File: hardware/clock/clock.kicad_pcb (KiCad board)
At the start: 4 copper layers, 106.7 x 76.2 mm, 101 parts, among them J1 Conn_Power, U1 74HC74, U10 74LVC1G38, U11 74LVC1G00, U12 74HC00, U13 74LVC1G38, U14 74HC02, U15 74LVC1G14, U16 74HC4017, U17 74HC4017, U19 74LVC1GX04, U2 74HCS05, U20 74LVC1G04, U21 NE555D, U22 74LVC1G32, U23 74LVC1G04, U24 MIC5504-3.3YM5, U25 74HC08, U26 74LVC2G132, U27 74HC74, U28 74LVC1G02, U29 74HC74, U3 74LVC1G02, U30 74LVC1G04, U4 74HCS05, U5 74LVC1G38, U6 74LVC2G74, U7 74LVC1G08, U8 74HC74, U9 74HCS05, Y1 Crystal

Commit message: Updated schematics and pcbs
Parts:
- removed C24: 100n, Capacitor_SMD:C_0805_2012Metric_Pad1.18x1.45mm_HandSolder
- added C18: 100n, Capacitor_SMD:C_0805_2012Metric_Pad1.18x1.45mm_HandSolder, B.Cu at (108.6, 146.1)
- added D2: LED, LED_SMD:LED_0805_2012Metric_Pad1.15x1.40mm_HandSolder, F.Cu at (98.4, 143.5)
- added D3: LED, LED_SMD:LED_0805_2012Metric_Pad1.15x1.40mm_HandSolder, F.Cu at (98.4, 146.1)
- added J2: Conn_01x03, Connector_PinHeader_2.54mm:PinHeader_1x03_P2.54mm_Vertical, F.Cu at (84.5, 101.6)
- added J3: Conn_01x02_Male, Connector_PinHeader_2.54mm:PinHeader_1x02_P2.54mm_Horizontal, F.Cu at (140.4, 115.6)
- added J4: Conn_01x02_Male, Connector_PinHeader_2.54mm:PinHeader_1x02_P2.54mm_Horizontal, F.Cu at (140.4, 136.5)
- added J5: Conn_01x10_Male, Connector_IDC:IDC-Header_2x05_P2.54mm_Vertical, F.Cu at (84.5, 145.4)
- added R27: 330, Resistor_SMD:R_0805_2012Metric_Pad1.20x1.40mm_HandSolder, B.Cu at (98.4, 143.5)
- added R28: 330, Resistor_SMD:R_0805_2012Metric_Pad1.20x1.40mm_HandSolder, B.Cu at (98.4, 146.1)
- added SW1: SW_Push_4pin, riscv-serial:SW_SPST_DTSM-6, F.Cu at (92.1, 82.5)
- added SW2: SW_Push_4pin, riscv-serial:SW_SPST_DTSM-6, F.Cu at (102.2, 82.5)
- added SW3: SW_Push_4pin, riscv-serial:SW_SPST_DTSM-6, F.Cu at (112.4, 82.5)
- added SW4: SW_Push_4pin, riscv-serial:SW_SPST_DTSM-6, F.Cu at (122.6, 82.5)
- added SW5: SW_Push_4pin, riscv-serial:SW_SPST_DTSM-6, F.Cu at (132.1, 82.5)
- added SW6: SW_Push_4pin, riscv-serial:SW_SPST_DTSM-6, F.Cu at (72.4, 132.1)
- added SW7: SW_Push_4pin, riscv-serial:SW_SPST_DTSM-6, F.Cu at (62.2, 85.7)
- added SW8: SW_Push_4pin, riscv-serial:SW_SPST_DTSM-6, F.Cu at (52.1, 85.7)
- added U18: 74LVC2G04, Package_TO_SOT_SMD:SOT-23-6_Handsoldering, B.Cu at (105.4, 144.8)
- C1, C10, C11, C12, C13, C14, C15, C16, C17, C19, C20, C21, C22, C23, C26, C27, C28, C29, C3, C30, C40, C41, C5, C6, C7, C8, J1, U24: moved to B.Cu
- moved J1 180.8 mm to (51.4, 139.1), turned to 90 degrees
- moved U24 166.2 mm to (64.1, 139.1)
- moved C40 166.0 mm to (59.7, 139.1), turned to 90 degrees
- moved C41 154.8 mm to (67.9, 139.1), turned to 90 degrees
- moved RV1 14.6 mm to (78.1, 91.8)
- moved R17 12.5 mm to (132.1, 91.4)
- moved C35 12.5 mm to (133.3, 94.8)
- moved R16 12.5 mm to (130.8, 94.9)
- moved C34 11.5 mm to (123.8, 94.8)
- moved R14 11.5 mm to (121.3, 94.9)
- moved R15 11.5 mm to (122.6, 91.4)
- moved C33 9.61 mm to (113.7, 94.8)
- moved R12 9.61 mm to (111.1, 94.9)
- moved R13 9.61 mm to (112.4, 91.4)
- moved R9 8.72 mm to (102.2, 90.8)
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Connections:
- U10 pad 1: /STEPDONE -> /STEP_DONE
- U5 pad 1: /OPDONE -> /OP_DONE
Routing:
- net /~{SLEEP}: track 15.4 -> 91.9 mm
- net /STEP_DONE: track 0.00 -> 44.5 mm, vias 0 -> 1
- net /~{CLK}: track 10.6 -> 48.5 mm, vias 0 -> 1
- net GND: track 98.7 -> 136.5 mm, vias 54 -> 51
- net /OP_DONE: track 0.00 -> 37.4 mm, vias 0 -> 1
- net /CLK: track 8.83 -> 46.1 mm, vias 0 -> 1
- net /~{RESET}: track 19.6 -> 46.1 mm
- net /B_OSC: track 10.6 -> 27.7 mm
- net /~{WAIT}: track 35.5 -> 18.6 mm
- net /B_555: track 9.89 -> 26.6 mm
- net /V_IN: track 0.00 -> 16.0 mm
- net /B_STOP: track 37.9 -> 51.3 mm, vias 0 -> 2
- net /B_RESET: track 0.00 -> 11.4 mm
- net Net-(C37-Pad1): track 15.2 -> 26.3 mm
- net Net-(R6-Pad2): track 0.00 -> 9.75 mm
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- added copper zone on B.Cu, net /V_IN
- added copper zone on B.Cu, net VCC
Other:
- board size 106.7 x 76.2 mm -> 99.1 x 76.2 mm
- board text added: "CLK"
- board text added: "~{CLK}"

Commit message: Updated PCBs
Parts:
- moved J5 19.6 mm to (100.3, 156.8)
- moved D2 1.91 mm to (96.5, 143.5)
- moved D3 1.91 mm to (96.5, 146.1)
- moved R27 1.91 mm to (96.5, 143.5)
- moved R28 1.91 mm to (96.5, 146.1)
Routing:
- net GND: track 136.5 -> 173.1 mm, vias 51 -> 60
- net /~{RESET}: track 46.1 -> 71.2 mm
- net /~{CLK}: track 48.5 -> 32.6 mm
- net /CLK: track 46.1 -> 30.7 mm
- net /~{SLEEP}: track 91.9 -> 79.7 mm
- net VCC: track 205.8 -> 217.8 mm, vias 44 -> 49
- net /OP_DONE: track 37.4 -> 45.7 mm
- net /STEP_DONE: track 44.5 -> 51.6 mm
- net Net-(D3-Pad1): track 3.05 -> 0.00 mm
- net Net-(D2-Pad1): track 3.05 -> 0.00 mm
- net Net-(R28-Pad2): track 5.07 -> 6.97 mm
- net Net-(R27-Pad2): track 8.49 -> 10.4 mm
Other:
- board size 99.1 x 76.2 mm -> 99.1 x 99.1 mm

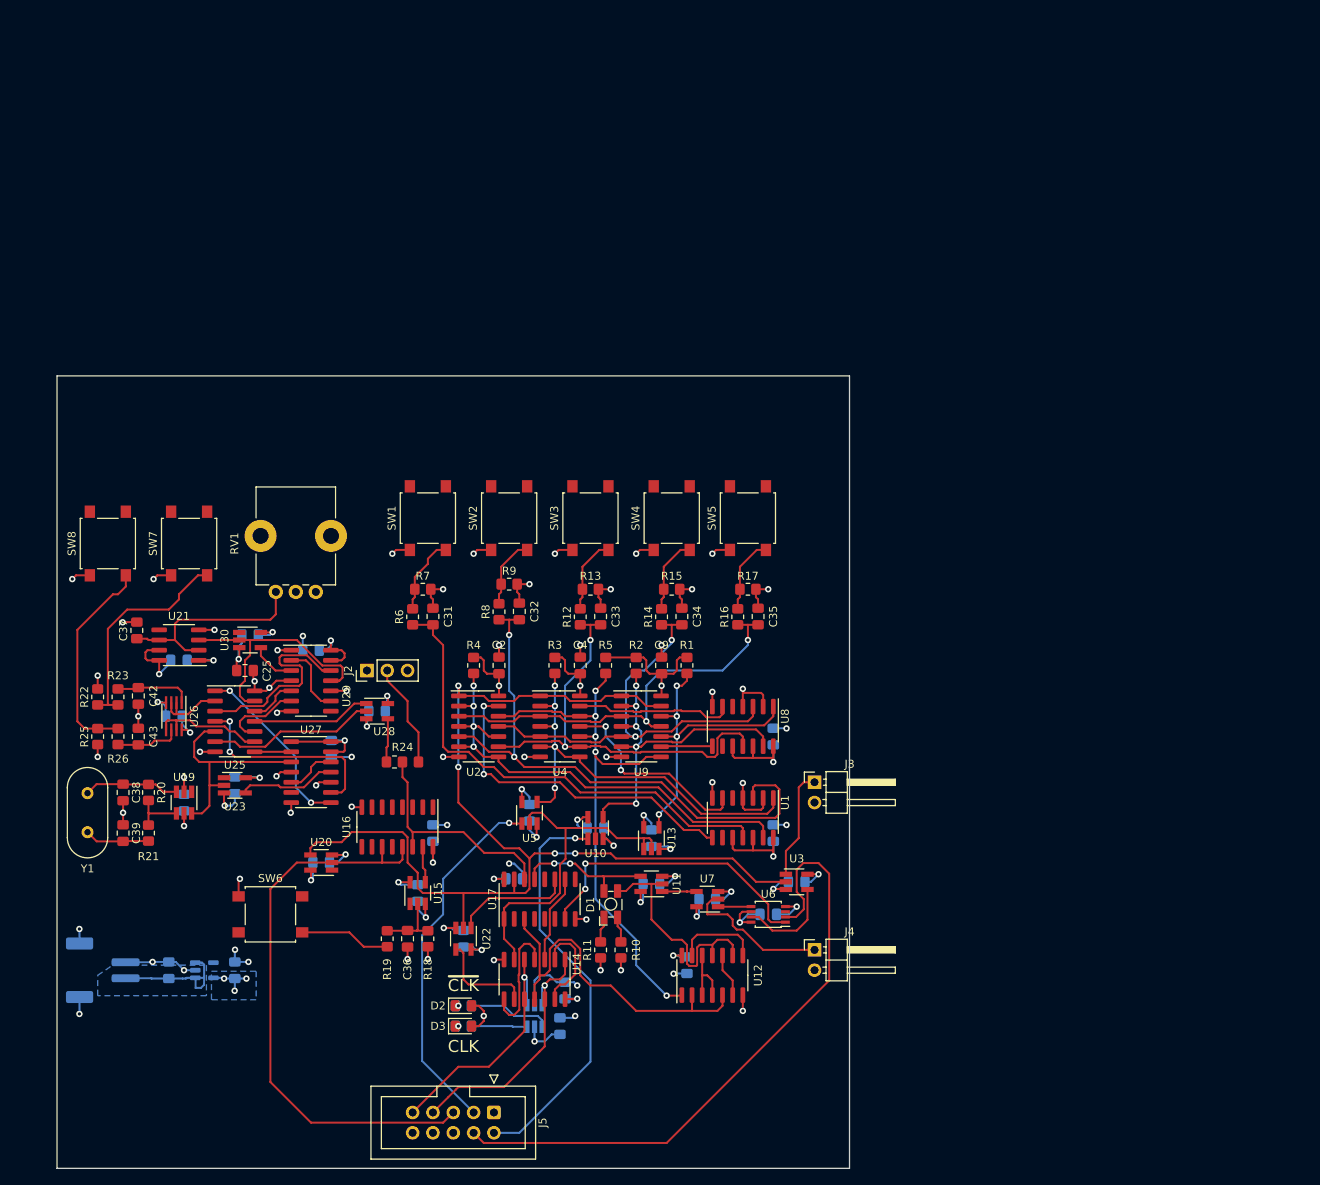
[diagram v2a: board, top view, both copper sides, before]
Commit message: Added two LEDs
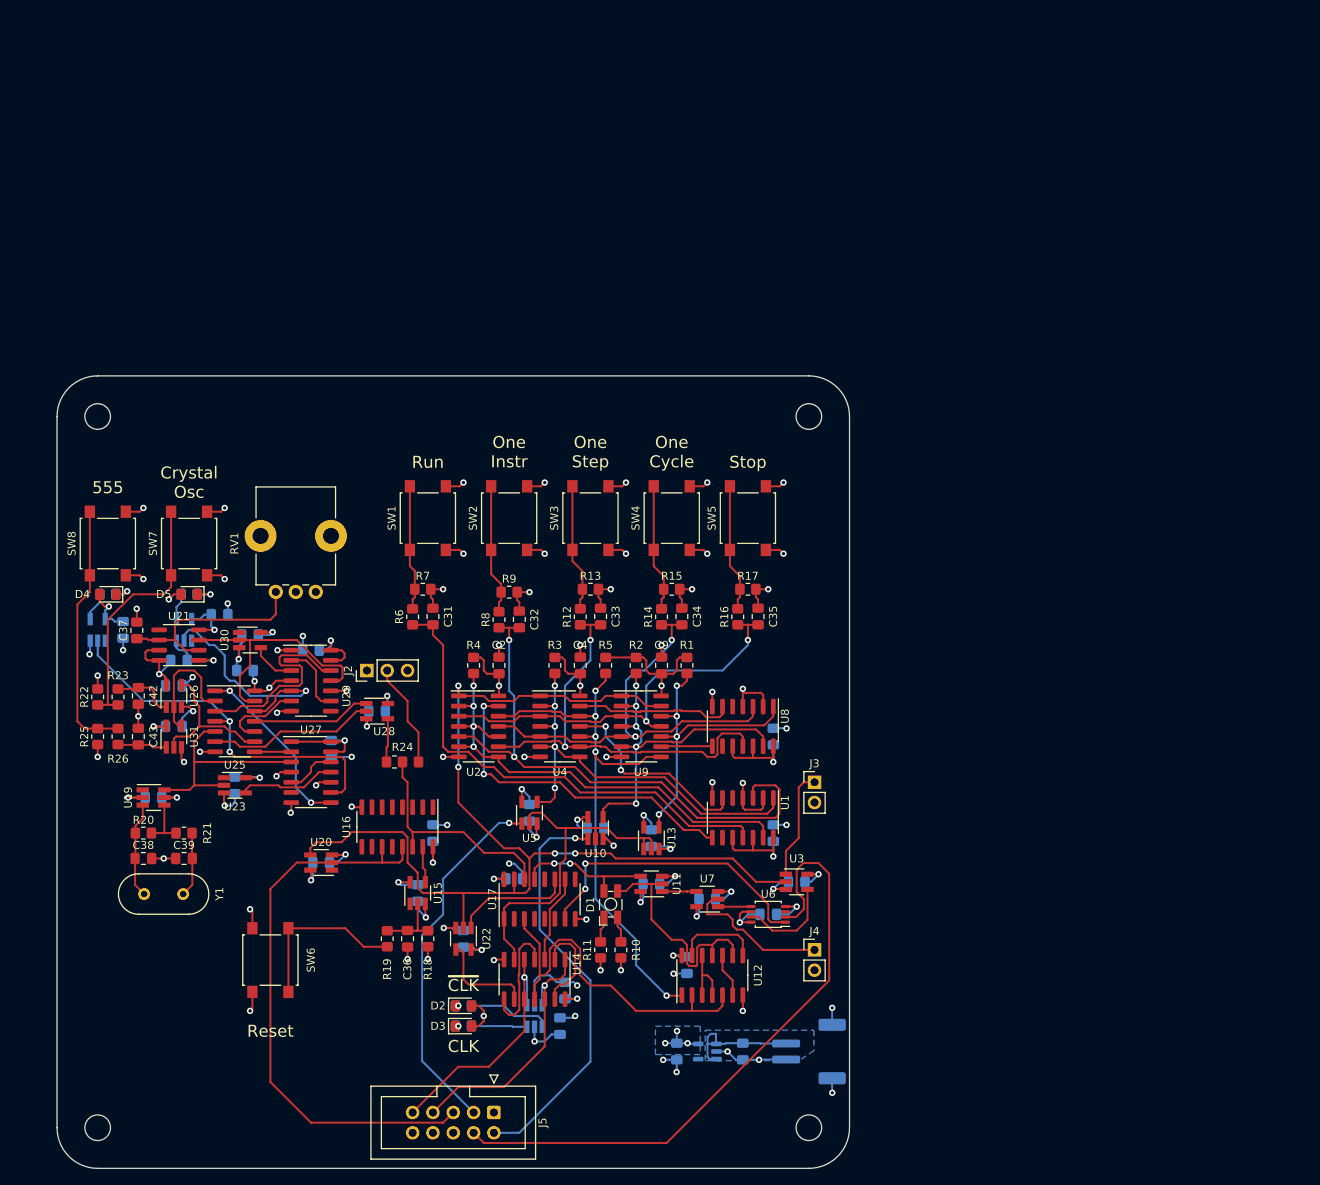
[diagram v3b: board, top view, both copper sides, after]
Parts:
- added C24: 100n, Capacitor_SMD:C_0805_2012Metric_Pad1.18x1.45mm_HandSolder, B.Cu at (60.3, 108.6)
- added C44: 100n, Capacitor_SMD:C_0805_2012Metric_Pad1.18x1.45mm_HandSolder, B.Cu at (66.0, 94.6)
- added C45: 100n, Capacitor_SMD:C_0805_2012Metric_Pad1.18x1.45mm_HandSolder, B.Cu at (54.0, 96.5)
- added D4: LED, LED_SMD:LED_0805_2012Metric_Pad1.15x1.40mm_HandSolder, F.Cu at (52.1, 92.1)
- added D5: LED, LED_SMD:LED_0805_2012Metric_Pad1.15x1.40mm_HandSolder, F.Cu at (62.2, 92.1)
- added R29: 330, Resistor_SMD:R_0805_2012Metric_Pad1.20x1.40mm_HandSolder, B.Cu at (52.1, 92.1)
- added R30: 330, Resistor_SMD:R_0805_2012Metric_Pad1.20x1.40mm_HandSolder, B.Cu at (62.2, 92.1)
- added REF**: MountingHole_3.2mm_M3, MountingHole:MountingHole_3.2mm_M3, F.Cu at (50.8, 158.8)
- added REF**: MountingHole_3.2mm_M3, MountingHole:MountingHole_3.2mm_M3, F.Cu at (139.7, 158.8)
- added REF**: MountingHole_3.2mm_M3, MountingHole:MountingHole_3.2mm_M3, F.Cu at (139.7, 69.8)
- added REF**: MountingHole_3.2mm_M3, MountingHole:MountingHole_3.2mm_M3, F.Cu at (50.8, 69.8)
- added U31: 74LVC1G132, Package_TO_SOT_SMD:SOT-23-5_HandSoldering, F.Cu at (60.3, 109.9)
- added U32: 74LVC1G04, Package_TO_SOT_SMD:SOT-23-5_HandSoldering, B.Cu at (50.8, 96.5)
- added U33: 74LVC1G04, Package_TO_SOT_SMD:SOT-23-5_HandSoldering, B.Cu at (61.6, 96.5)
- C25: moved to B.Cu
- J3, J4: footprint Connector_PinHeader_2.54mm:PinHeader_1x02_P2.54mm_Horizontal -> Connector_PinHeader_2.54mm:PinHeader_1x02_P2.54mm_Vertical
- U26: value 74LVC2G132 -> 74LVC1G132; footprint Package_SO:SSOP-8_2.95x2.8mm_P0.65mm -> Package_TO_SOT_SMD:SOT-23-5_HandSoldering
- moved J1 88.8 mm to (139.7, 149.2), turned to -90 degrees
- moved C40 72.5 mm to (131.4, 149.2), turned to -90 degrees
- moved U24 63.7 mm to (127.0, 149.2), turned to 180 degrees
- moved C41 56.2 mm to (123.2, 149.2), turned to -90 degrees
- moved Y1 14.5 mm to (56.6, 129.5), turned to 0 degrees
- moved C38 8.64 mm to (56.5, 125.1), turned to 0 degrees
- moved C39 8.25 mm to (61.6, 125.1), turned to 180 degrees
- moved SW6 5.71 mm to (72.4, 137.8), turned to 90 degrees
- moved R20 5.12 mm to (56.5, 121.9), turned to 0 degrees
- moved R21 4.45 mm to (61.6, 121.9), turned to 180 degrees
- moved C19 3.86 mm to (57.8, 117.5), turned to 180 degrees
- moved U19 3.86 mm to (57.8, 117.5), turned to 0 degrees
- moved C26 3.81 mm to (60.3, 103.5), turned to 0 degrees
- moved U26 2.54 mm to (60.3, 104.8), turned to 90 degrees
- moved C32 1.00 mm to (103.5, 95.2)
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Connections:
- SW1 pad 1: VCC -> Net-(R6-Pad2)
- SW1 pad 2: unconnected-(SW1-Pad2) -> Net-(R6-Pad2)
- SW1 pad 3: Net-(R6-Pad2) -> VCC
- SW1 pad 4: unconnected-(SW1-Pad4) -> VCC
- SW2 pad 1: VCC -> Net-(R8-Pad2)
- SW2 pad 2: unconnected-(SW2-Pad2) -> Net-(R8-Pad2)
- SW2 pad 3: Net-(R8-Pad2) -> VCC
- SW2 pad 4: unconnected-(SW2-Pad4) -> VCC
- SW3 pad 1: VCC -> Net-(R12-Pad2)
- SW3 pad 2: unconnected-(SW3-Pad2) -> Net-(R12-Pad2)
- SW3 pad 3: Net-(R12-Pad2) -> VCC
- SW3 pad 4: unconnected-(SW3-Pad4) -> VCC
- SW4 pad 1: VCC -> Net-(R14-Pad2)
- SW4 pad 2: unconnected-(SW4-Pad2) -> Net-(R14-Pad2)
- SW4 pad 3: Net-(R14-Pad2) -> VCC
- SW4 pad 4: unconnected-(SW4-Pad4) -> VCC
- SW5 pad 1: VCC -> Net-(R16-Pad2)
- SW5 pad 2: unconnected-(SW5-Pad2) -> Net-(R16-Pad2)
- SW5 pad 3: Net-(R16-Pad2) -> VCC
- SW5 pad 4: unconnected-(SW5-Pad4) -> VCC
- SW6 pad 2: unconnected-(SW6-Pad2) -> GND
- SW6 pad 3: unconnected-(SW6-Pad3) -> /B_RESET
- SW7 pad 1: GND -> /B_OSC
- SW7 pad 2: unconnected-(SW7-Pad2) -> /B_OSC
- SW7 pad 3: /B_OSC -> GND
- SW7 pad 4: unconnected-(SW7-Pad4) -> GND
- SW8 pad 1: GND -> /B_555
- SW8 pad 2: unconnected-(SW8-Pad2) -> /B_555
- SW8 pad 3: /B_555 -> GND
- SW8 pad 4: unconnected-(SW8-Pad4) -> GND
- U26 pad 3: Net-(U25-Pad2) -> GND
- U26 pad 4: GND -> Net-(U25-Pad9)
- U26 pad 5: Net-(U25-Pad9) -> VCC
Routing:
- net VCC: track 217.8 -> 246.0 mm, vias 49 -> 56
- net Net-(U25-Pad12): track 6.00 -> 29.2 mm, vias 0 -> 1
- net Net-(U25-Pad4): track 26.0 -> 47.8 mm
- net GND: track 173.1 -> 192.9 mm, vias 60 -> 68
- net /B_RESET: track 11.4 -> 21.3 mm
- net Net-(R8-Pad2): track 8.85 -> 16.3 mm
- net Net-(U25-Pad2): track 8.88 -> 15.4 mm
- net Net-(R12-Pad2): track 9.49 -> 15.9 mm
- net Net-(R16-Pad2): track 9.49 -> 15.9 mm
- net Net-(R14-Pad2): track 9.49 -> 15.9 mm
- net Net-(R6-Pad2): track 9.75 -> 15.7 mm
- net /B_555: track 26.6 -> 32.3 mm
- net Net-(U25-Pad9): track 14.5 -> 19.2 mm
- net /B_OSC: track 27.7 -> 32.3 mm
- net Net-(R29-Pad2): track 0.00 -> 3.60 mm
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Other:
- outline, holes or cut-outs redrawn
- board text added: "555"
- board text added: "Crystal Osc"
- board text added: "One Cycle"
- board text added: "One Instr"
- board text added: "One Step"
- board text added: "Reset"
- board text added: "Run"
- board text added: "Stop"
